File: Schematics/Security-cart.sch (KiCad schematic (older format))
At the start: 4 parts

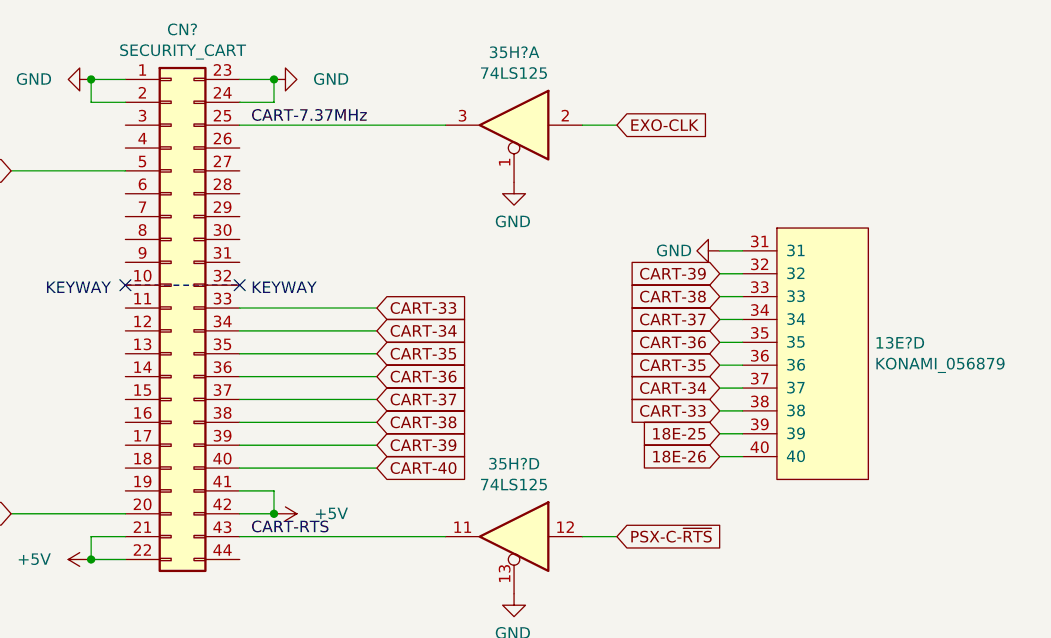
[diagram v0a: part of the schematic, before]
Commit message: Added GE675-PWB(A)
IO Board for Fisherman's Bait 3
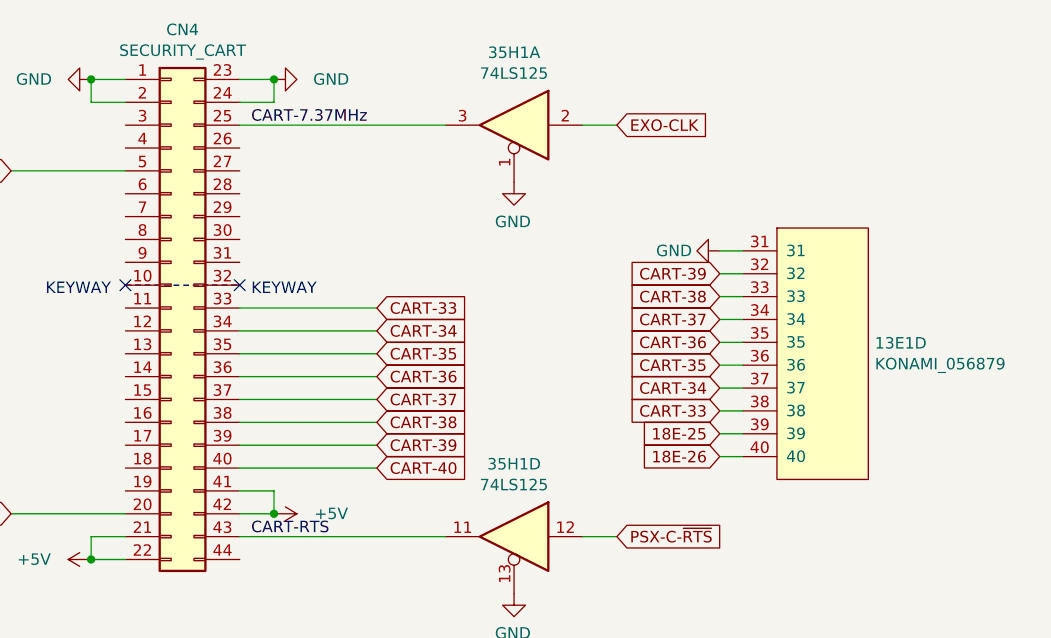
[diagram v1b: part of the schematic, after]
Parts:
- gave numbers to parts that had none: 3
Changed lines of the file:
@@
 $EndDescr
 $Comp
-L Arcade:KONAMI_056879 13E?
+L Arcade:KONAMI_056879 13E1
 U 4 1 64B0B54B
 P 7500 4500
-F 0 "13E?" H 7728 5196 50  0000 L CNN
+F 0 "13E1" H 7728 5196 50  0000 L CNN
 F 1 "KONAMI_056879" H 7728 5105 50  0000 L CNN
 F 2 "Package_QFP:TQFP-120_14x14mm_P0.4mm" H 7500 4500 50  0001 C CNN
@@
 $EndComp
 $Comp
-L power:GND #PWR?
+L power:GND #PWR0168
 U 1 1 64B0B551
 P 7050 3400
-F 0 "#PWR?" H 7050 3150 50  0001 C CNN
+F 0 "#PWR0168" H 7050 3150 50  0001 C CNN
 F 1 "GND" V 7050 3200 50  0000 C CNN
 F 2 "" H 7050 3400 50  0001 C CNN
@@
 	7050 3500 7150 3500
 $Comp
-L 74xx:74LS125 35H?
+L 74xx:74LS125 35H1
 U 1 1 64B0B56A
 P 6150 2850
-F 0 "35H?" H 6150 3167 50  0000 C CNN
+F 0 "35H1" H 6150 3167 50  0000 C CNN
 F 1 "74LS125" H 6150 3076 50  0000 C CNN
 F 2 "Package_SO:SO-14_3.9x8.65mm_P1.27mm" H 6150 2850 50  0001 C CNN
@@
 $EndComp
 $Comp
-L 74xx:74LS125 35H?
+L 74xx:74LS125 35H1
 U 4 1 64B0B570
 P 6150 4650
-F 0 "35H?" H 6150 4967 50  0000 C CNN
+F 0 "35H1" H 6150 4967 50  0000 C CNN
 F 1 "74LS125" H 6150 4876 50  0000 C CNN
 F 2 "Package_SO:SO-14_3.9x8.65mm_P1.27mm" H 6150 4650 50  0001 C CNN
@@
 $EndComp
 $Comp
-L power:GND #PWR?
+L power:GND #PWR0169
 U 1 1 64B0B576
 P 6150 3100
-F 0 "#PWR?" H 6150 2850 50  0001 C CNN
+F 0 "#PWR0169" H 6150 2850 50  0001 C CNN
 F 1 "GND" H 6155 2927 50  0000 C CNN
 F 2 "" H 6150 3100 50  0001 C CNN
@@
 $EndComp
 $Comp
-L power:GND #PWR?
+L power:GND #PWR0170
 U 1 1 64B0B57C
 P 6150 4900
-F 0 "#PWR?" H 6150 4650 50  0001 C CNN
+F 0 "#PWR0170" H 6150 4650 50  0001 C CNN
 F 1 "GND" H 6155 4727 50  0000 C CNN
 F 2 "" H 6150 4900 50  0001 C CNN
@@
 CART-RTS
 $Comp
-L power:GND #PWR?
+L power:GND #PWR0171
 U 1 1 64B0B58A
 P 4300 2650
-F 0 "#PWR?" H 4300 2400 50  0001 C CNN
+F 0 "#PWR0171" H 4300 2400 50  0001 C CNN
 F 1 "GND" V 4300 2400 50  0000 C CNN
 F 2 "" H 4300 2650 50  0001 C CNN
@@
 	4300 2650 4450 2650
 $Comp
-L power:GND #PWR?
+L power:GND #PWR0172
 U 1 1 64B0B594
 P 5100 2650
-F 0 "#PWR?" H 5100 2400 50  0001 C CNN
+F 0 "#PWR0172" H 5100 2400 50  0001 C CNN
 F 1 "GND" V 5100 2400 50  0000 C CNN
 F 2 "" H 5100 2650 50  0001 C CNN
@@
 	5100 2650 4950 2650
 $Comp
-L power:+5V #PWR?
+L power:+5V #PWR0173
 U 1 1 64B0B59E
 P 4300 4750
-F 0 "#PWR?" H 4300 4600 50  0001 C CNN
+F 0 "#PWR0173" H 4300 4600 50  0001 C CNN
 F 1 "+5V" V 4300 5000 50  0000 C CNN
 F 2 "" H 4300 4750 50  0001 C CNN
@@
 Connection ~ 4300 4750
 $Comp
-L power:+5V #PWR?
+L power:+5V #PWR0174
 U 1 1 64B0B5A8
 P 5100 4550
-F 0 "#PWR?" H 5100 4400 50  0001 C CNN
+F 0 "#PWR0174" H 5100 4400 50  0001 C CNN
 F 1 "+5V" V 5100 4800 50  0000 C CNN
 F 2 "" H 5100 4550 50  0001 C CNN
@@
 	4950 3850 5550 3850
 $Comp
-L Connector_Generic:Conn_02x22_Top_Bottom CN?
+L Connector_Generic:Conn_02x22_Top_Bottom CN4
 U 1 1 64B0B5C2
 P 4650 3650
-F 0 "CN?" H 4700 4867 50  0000 C CNN
+F 0 "CN4" H 4700 4867 50  0000 C CNN
 F 1 "SECURITY_CART" H 4700 4776 50  0000 C CNN
 F 2 "" H 4650 3650 50  0001 C CNN

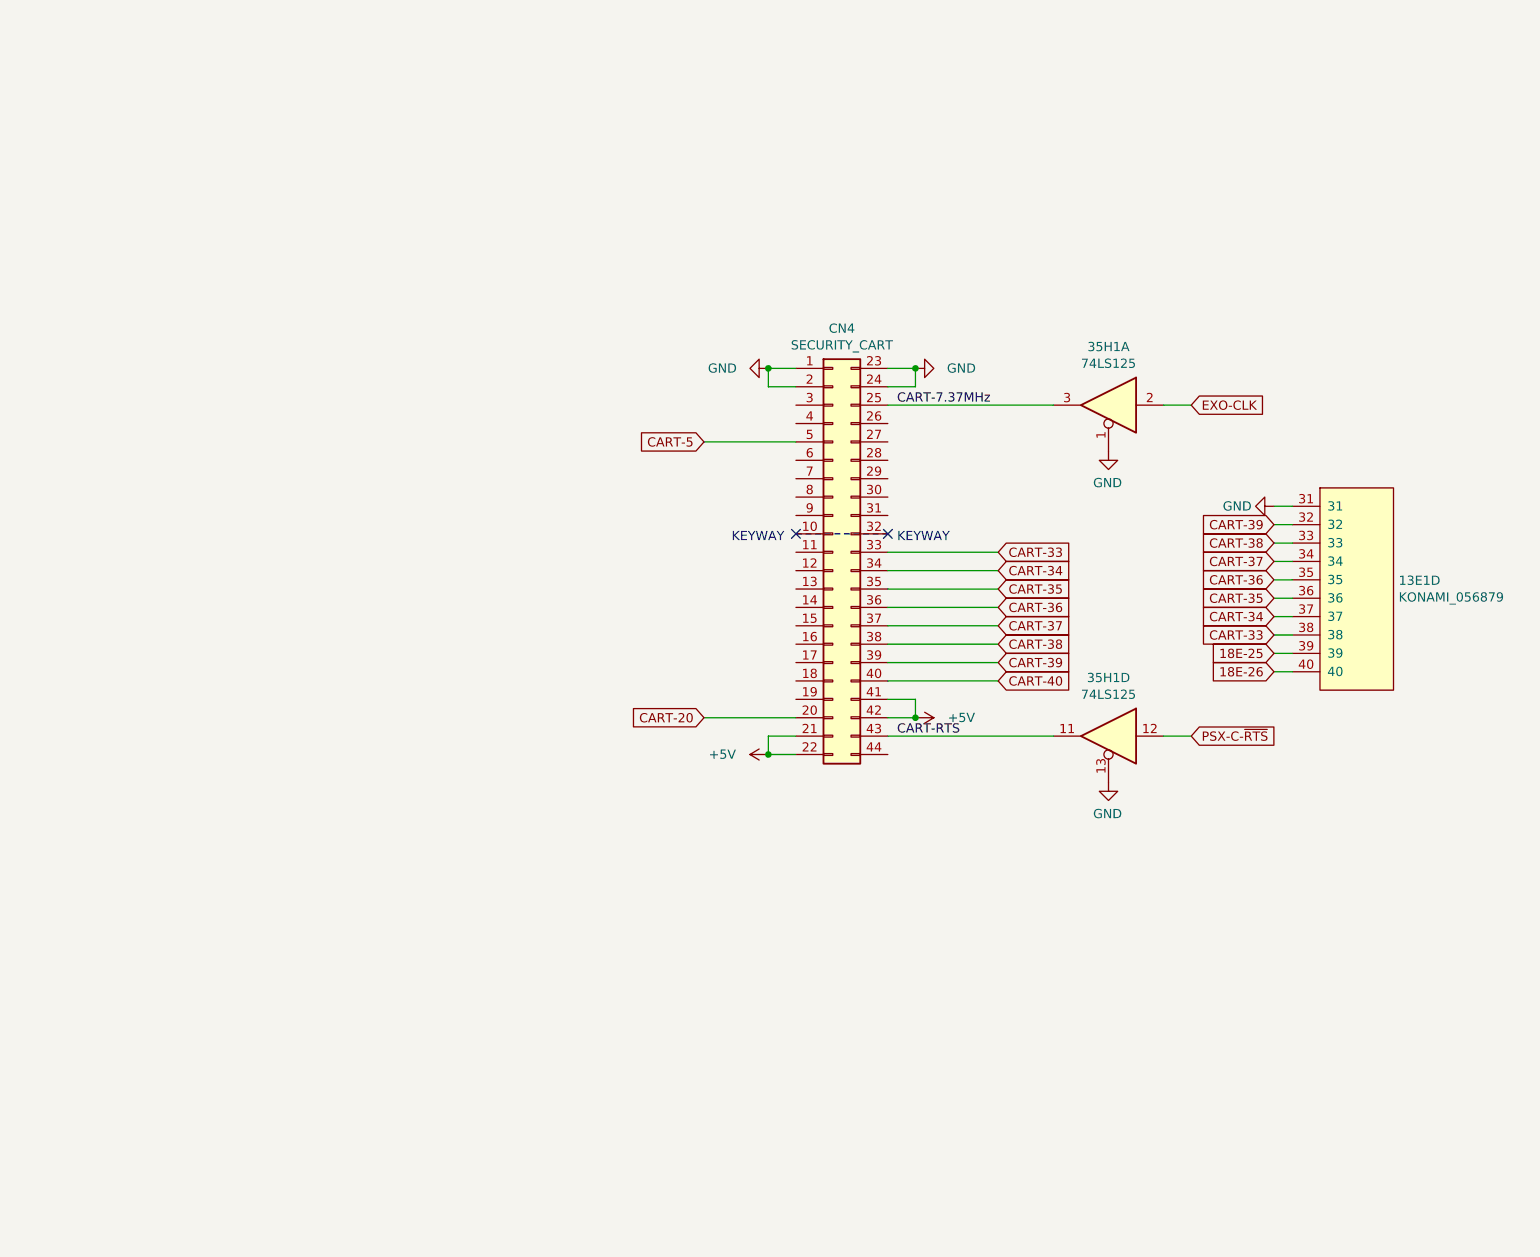
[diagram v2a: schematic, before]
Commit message: Flash fixes, security cart done, most logic figured
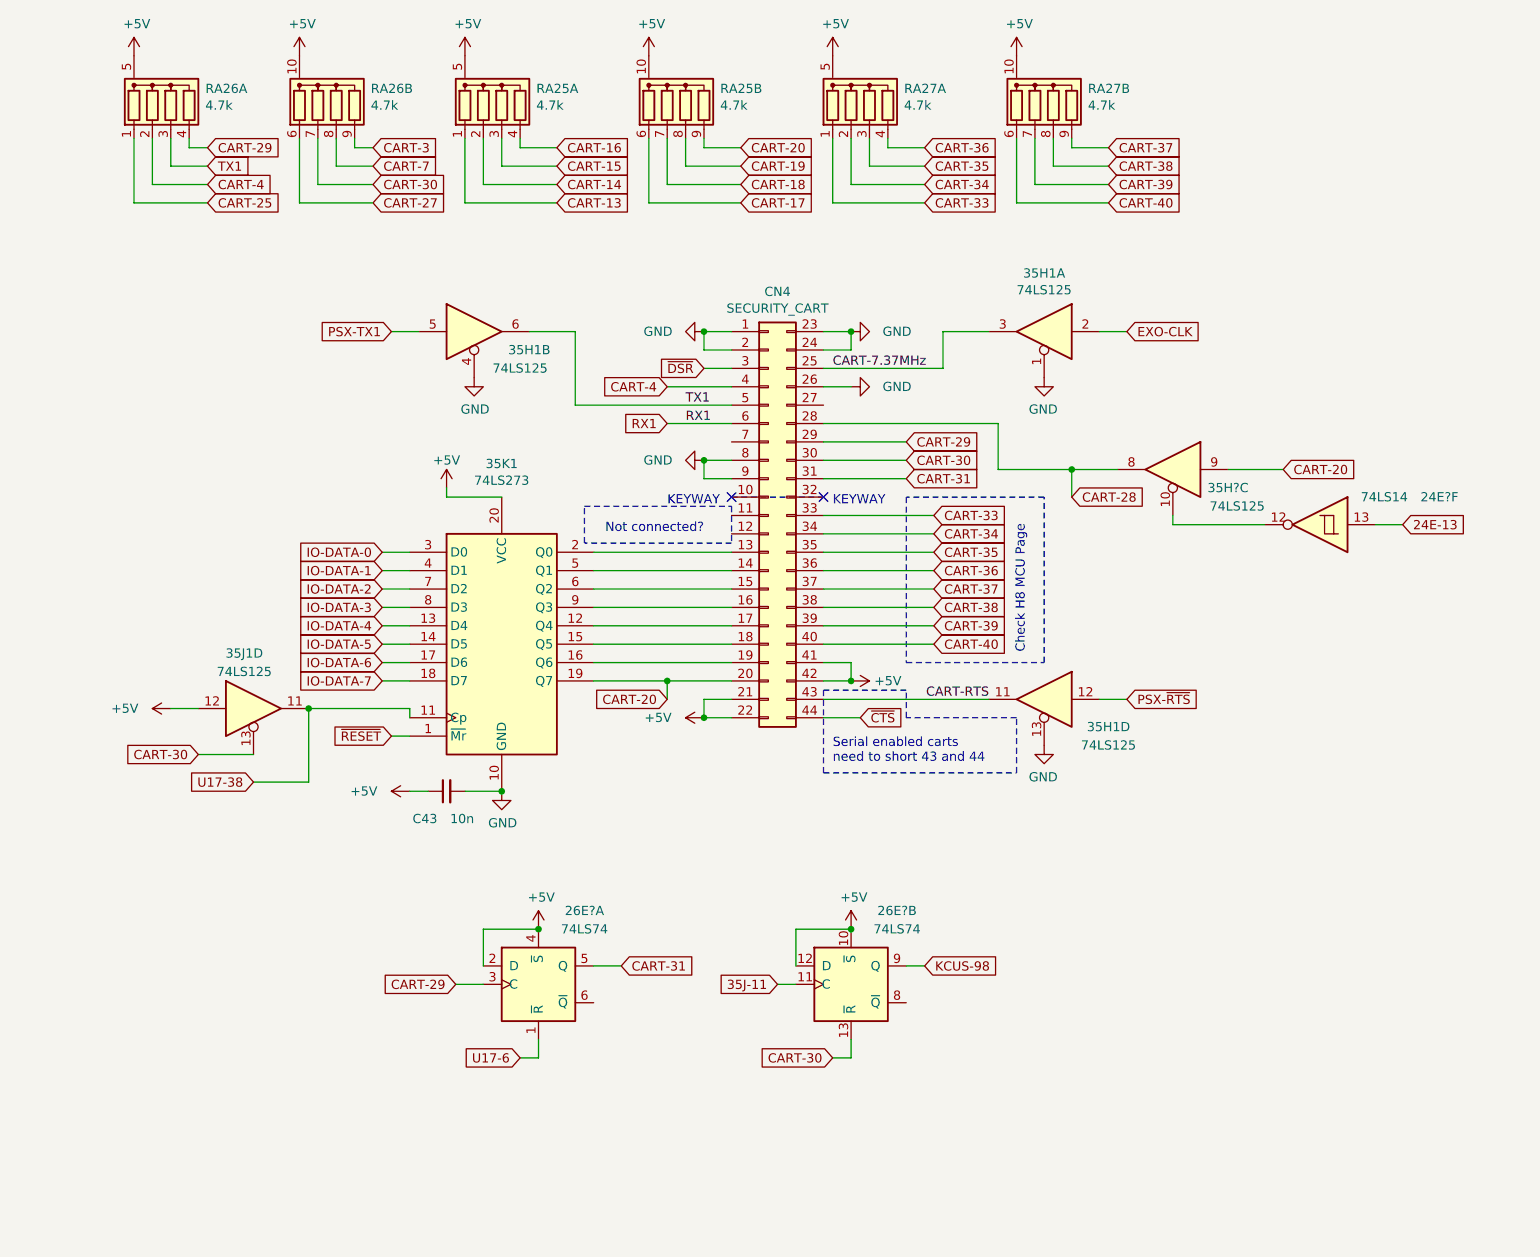
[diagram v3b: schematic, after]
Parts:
- removed 13E1: KONAMI_056879, Package_QFP:TQFP-120_14x14mm_P0.4mm, symbol Arcade:KONAMI_056879
- added 24E?: 74LS14, Package_SO:SO-14_3.9x8.65mm_P1.27mm, symbol 74xx:74LS14
- added 26E? (x2): 74LS74, Package_SO:SO-14_3.9x8.65mm_P1.27mm, symbol 74xx:74LS74
- added unit 2 of 35H1
- added 35H?, 35J1: 74LS125, Package_SO:SO-14_3.9x8.65mm_P1.27mm, symbol 74xx:74LS125
- added 35K1: 74LS273, Package_SO:SO-20_5.3x12.6mm_P1.27mm, symbol 74xx:74LS273
- added C43: 10n, Capacitor_SMD:C_0805_2012Metric, symbol Device:C_Small
- added RA25, RA26, RA27: 4.7k, Resistor_SMD:R_Array_Convex_5x1206, symbol Device:R_Dual_Network08_Split
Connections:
- net +5V: now also 26E?.10 (~S), 26E?.12 (D), 26E?.2 (D), 26E?.4 (~S), 35J1.12, 35K1.20 (VCC), C43.1, RA25.10 (common), RA25.5 (common), RA26.10 (common), RA26.5 (common), RA27.10 (common), RA27.5 (common)
- net CART-20: now also 35H?.9, 35K1.19 (Q7), RA25.9 (R8)
- net CART-33: now also RA27.1 (R1)
- net CART-34: now also RA27.2 (R2)
- net CART-35: now also RA27.3 (R3)
- net CART-36: now also RA27.4 (R4)
- net CART-37: now also RA27.9 (R8)
- net CART-38: now also RA27.8 (R7)
- net CART-39: now also RA27.7 (R6)
- net CART-40: now also RA27.6 (R5)
- net GND: now also CN4.26 (Pin_26), CN4.8 (Pin_8), CN4.9 (Pin_9), 35H1.4, 35K1.10 (GND), C43.2
- net at CN4.13 (Pin_13): now also 35K1.2 (Q0)
- net at CN4.14 (Pin_14): now also 35K1.5 (Q1)
- net at CN4.15 (Pin_15): now also 35K1.6 (Q2)
- net at CN4.16 (Pin_16): now also 35K1.9 (Q3)
- net at CN4.17 (Pin_17): now also 35K1.12 (Q4)
- net at CN4.18 (Pin_18): now also 35K1.15 (Q5)
- net at CN4.19 (Pin_19): now also 35K1.16 (Q6)
- net CART-28: now reaches CN4.28 (Pin_28)
- net CART-28: now also 35H?.8
- net CART-29: now reaches CN4.29 (Pin_29)
- net CART-29: now also 26E?.3 (C), RA26.4 (R4)
- net ~DSR: now reaches CN4.3 (Pin_3)
- net CART-30: now reaches CN4.30 (Pin_30)
- net CART-30: now also 26E?.13 (~R), 35J1.13, RA26.7 (R6)
- net CART-31: now reaches CN4.31 (Pin_31)
- net CART-31: now also 26E?.5 (Q)
- net CART-4: now reaches CN4.4 (Pin_4)
- net CART-4: now also RA26.2 (R2)
- net ~CTS: now reaches CN4.44 (Pin_44)
- net RX1: now reaches CN4.6 (Pin_6)
- net CART-5 renamed TX1
- net TX1: now also 35H1.6, RA26.3 (R3)
- net PSX-C-~RTS renamed PSX-~RTS
- new net: 24E?.12, 35H?.10
- new net 24E-13: 24E?.13
- new net 35J-11: 26E?.11 (C)
- new net CART-13: RA25.1 (R1)
- new net CART-14: RA25.2 (R2)
- new net CART-15: RA25.3 (R3)
- new net CART-16: RA25.4 (R4)
- new net CART-17: RA25.6 (R5)
- new net CART-18: RA25.7 (R6)
- new net CART-19: RA25.8 (R7)
- new net CART-25: RA26.1 (R1)
- new net CART-27: RA26.6 (R5)
- new net CART-3: RA26.9 (R8)
- new net CART-7: RA26.8 (R7)
- new net IO-DATA-0: 35K1.3 (D0)
- new net IO-DATA-1: 35K1.4 (D1)
- new net IO-DATA-2: 35K1.7 (D2)
- new net IO-DATA-3: 35K1.8 (D3)
- new net IO-DATA-4: 35K1.13 (D4)
- new net IO-DATA-5: 35K1.14 (D5)
- new net IO-DATA-6: 35K1.17 (D6)
- new net IO-DATA-7: 35K1.18 (D7)
- new net KCUS-98: 26E?.9 (Q)
- new net PSX-TX1: 35H1.5
- new net U17-38: 35J1.11, 35K1.11 (Cp)
- new net U17-6: 26E?.1 (~R)
- new net ~RESET: 35K1.1 (~Mr)
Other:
- note added: "Check H8 MCU Page"
- note added: "Not connected?"
- note added: "Serial enabled carts\nneed to short 43 and 44"
- moved on the sheet: 35H1A, 35H1D, CN4

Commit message: 573 specific mostly mapped
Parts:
- gave numbers to parts that had none: 1
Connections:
- net CART-27 is gone; now on net 35J-9: RA26.6 (R5)
- net KCUS-98 is gone; now on net 35J-9: 35J.9 (Q)
- net CART-20: now also 35K1.2 (Q0); no longer 35K1.19 (Q7)
- net at CN4.13 (Pin_13): now also 35K1.19 (Q7); no longer 35K1.2 (Q0)
- net at CN4.14 (Pin_14): now also 35K1.16 (Q6); no longer 35K1.5 (Q1)
- net at CN4.15 (Pin_15): now also 35K1.15 (Q5); no longer 35K1.6 (Q2)
- net at CN4.16 (Pin_16): now also 35K1.12 (Q4); no longer 35K1.9 (Q3)
- net at CN4.17 (Pin_17): now also 35K1.9 (Q3); no longer 35K1.12 (Q4)
- net at CN4.18 (Pin_18): now also 35K1.6 (Q2); no longer 35K1.15 (Q5)
- net at CN4.19 (Pin_19): now also 35K1.5 (Q1); no longer 35K1.16 (Q6)
- net 35J-9: now reaches CN4.27 (Pin_27)
- net CART-31 renamed 35J-5
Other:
- note added: "In port"
- note added: "KCUS 97"
- note added: "KCUS 98"
- note added: "Output port"
- moved on the sheet: 35J1D, 35JA, 35JB, 35K1, C43
